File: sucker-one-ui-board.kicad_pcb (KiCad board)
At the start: 2 copper layers, 36.4 x 48.3 mm, 32 parts, among them J1 52271-1079, Q1 BSS138, SW1 LIFT, SW2 LOW, SW3 REVERSE, SW4 TRIGGER, SW5 DROP, SW6 HIGH, U1 WS2812-2020, U10 WS2812-2020, U11 WS2812-2020, U12 WS2812-2020, U2 WS2812-2020, U3 WS2812-2020, U4 WS2812-2020, U5 WS2812-2020, U6 WS2812-2020, U7 WS2812-2020, U8 WS2812-2020, U9 WS2812-2020

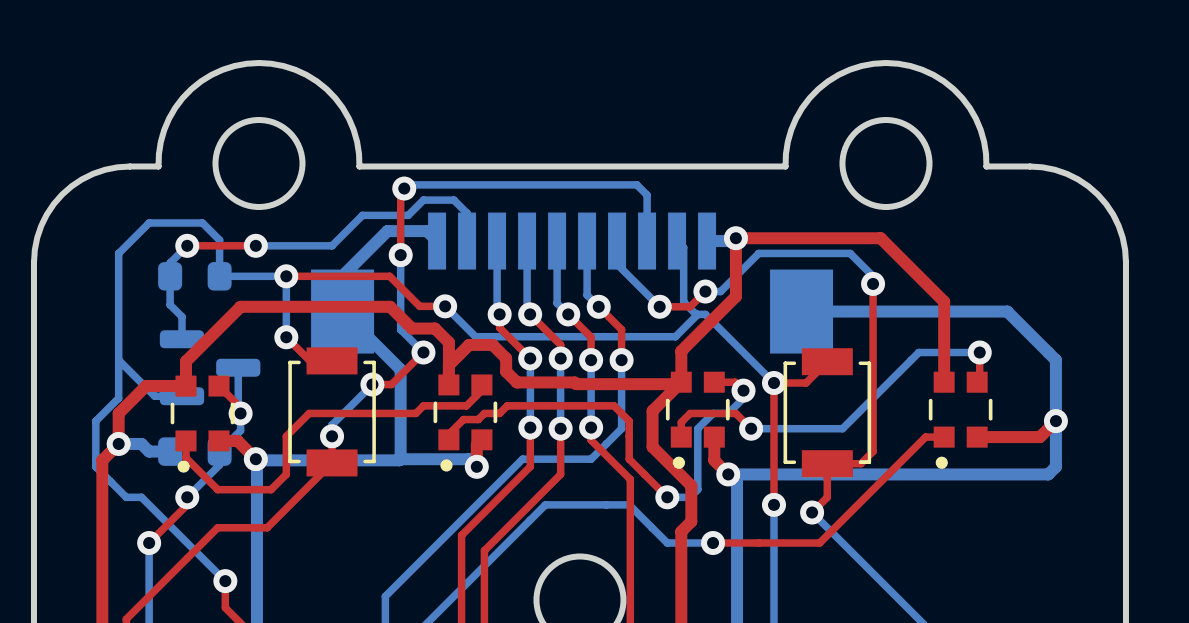
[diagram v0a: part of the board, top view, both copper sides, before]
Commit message: Flipped FFC connector and generated gerbers
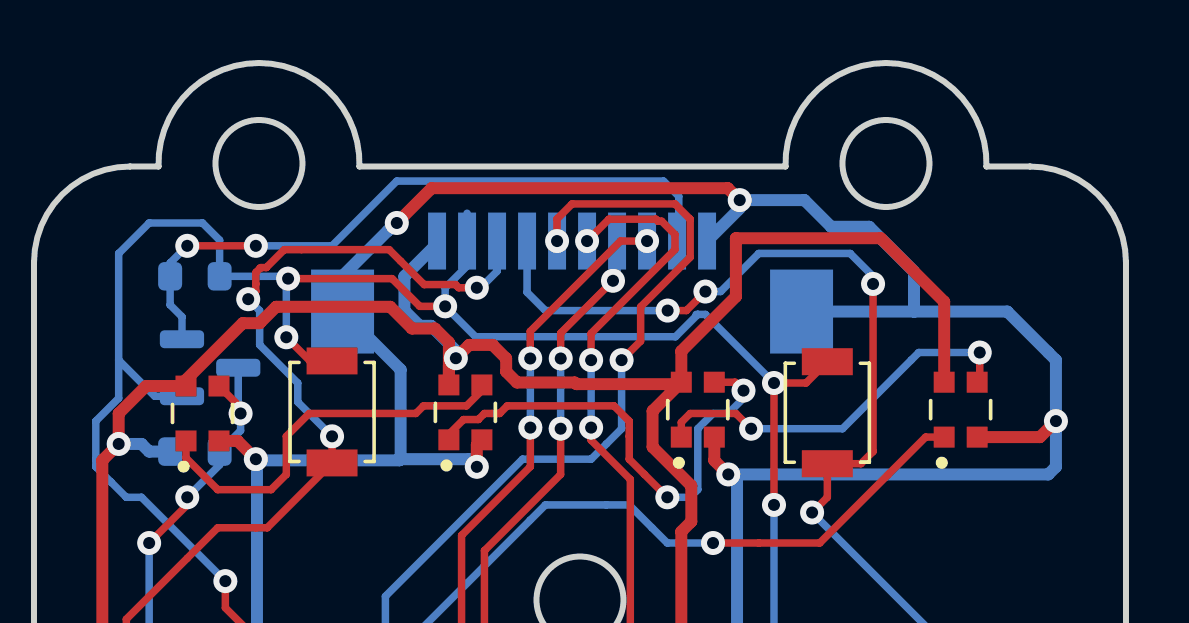
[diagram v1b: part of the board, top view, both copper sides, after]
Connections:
- J1 pad 1: +5V -> GND
- J1 pad 10: GND -> +5V
- J1 pad 2: +3V3 -> DATA_IN
- J1 pad 3: LIFT_BTN -> TRIGGER_BTN
- J1 pad 4: DROP_BTN -> REVERSE_BTN
- J1 pad 5: LOW_BTN -> HIGH_BTN
- J1 pad 6: HIGH_BTN -> LOW_BTN
- J1 pad 7: REVERSE_BTN -> DROP_BTN
- J1 pad 8: TRIGGER_BTN -> LIFT_BTN
- J1 pad 9: Net-(J1-Pad9) -> +3V3
- Q1 pad 2: Net-(J1-Pad9) -> DATA_IN
- R1 pad 1: Net-(J1-Pad9) -> DATA_IN
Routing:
- net DATA_IN: track 0.00 -> 22.5 mm, vias 0 -> 2
- net GND: track 162.8 -> 183.5 mm, vias 15 -> 17
- net Net-(J1-Pad9): track 15.4 -> 0.00 mm, vias 2 -> 0
- net LOW_BTN: track 68.9 -> 75.7 mm
- net HIGH_BTN: track 45.1 -> 49.5 mm
- net +5V: track 158.4 -> 162.3 mm
- net DROP_BTN: track 68.6 -> 72.3 mm
- net LIFT_BTN: track 65.3 -> 62.2 mm, vias 8 -> 6
- net TRIGGER_BTN: track 44.9 -> 46.6 mm
- net +3V3: track 105.1 -> 106.6 mm
- net REVERSE_BTN: track 65.1 -> 66.2 mm
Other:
- board text added: "5V"

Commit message: Updated and ordered ref 2
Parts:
- added C1: 100n, Capacitor_SMD:C_0603_1608Metric, F.Cu at (90.2, 89.9)
- added C2: 100n, Capacitor_SMD:C_0603_1608Metric, F.Cu at (73.6, 77.4)
- added C3: 100n, Capacitor_SMD:C_0603_1608Metric, F.Cu at (90.2, 77.4)
- added C4: 100n, Capacitor_SMD:C_0603_1608Metric, F.Cu at (73.6, 90.0)
- added C5: 100n, Capacitor_SMD:C_0603_1608Metric, F.Cu at (90.2, 102.4)
- added C6: 100n, Capacitor_SMD:C_0603_1608Metric, F.Cu at (73.6, 102.4)
- added C7: 50p, Capacitor_SMD:C_0603_1608Metric, B.Cu at (91.7, 69.6)
- moved TP8 39.0 mm to (66.4, 78.1)
- moved TP4 27.8 mm to (94.8, 77.7)
- moved TP2 27.6 mm to (69.2, 78.1)
- moved TP3 23.7 mm to (68.7, 90.3)
- moved TP5 22.5 mm to (68.7, 103.7)
- moved TP6 15.1 mm to (94.8, 90.8)
- moved TP10 9.31 mm to (69.5, 93.6)
- moved TP9 9.31 mm to (72.1, 93.6)
- moved TP1 9.31 mm to (74.6, 93.6)
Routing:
- net GND: track 183.5 -> 50.2 mm, vias 17 -> 28
- net +5V: track 162.3 -> 31.4 mm, vias 3 -> 21
- net LED_DATA: track 63.0 -> 10.7 mm, vias 3 -> 1
- net DROP_BTN: track 72.3 -> 24.3 mm, vias 6 -> 4
- net LIFT_BTN: track 62.2 -> 16.5 mm, vias 6 -> 2
- net LOW_BTN: track 75.7 -> 33.8 mm, vias 10 -> 6
- net HIGH_BTN: track 49.5 -> 30.6 mm, vias 6 -> 5
- net +3V3: track 106.6 -> 123.1 mm, vias 14 -> 3
- net DATA_IN: track 22.5 -> 34.4 mm, vias 2 -> 0
- net REVERSE_BTN: track 66.2 -> 58.0 mm
- net DO_LIFT: track 16.3 -> 11.9 mm, vias 2 -> 0
- net TRIGGER_BTN: track 46.6 -> 42.8 mm, vias 6 -> 5
- net Net-(U3-Pad1): track 14.5 -> 11.1 mm, vias 2 -> 0
- net Net-(U12-Pad3): track 10.9 -> 14.2 mm, vias 2 -> 0
- net Net-(U11-Pad3): track 11.2 -> 13.8 mm, vias 2 -> 0
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- added copper zone on In2.Cu, net +5V
- added copper zone on In1.Cu, net GND
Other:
- copper layers 2 -> 4
- board text added: "LED Orientation"
- board text removed: "Sucker One UI Board v1.0"

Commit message: Refactorings
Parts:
- removed Q1: BSS138, Package_TO_SOT_SMD:SOT-23
- removed R1, R2: 10k, Resistor_SMD:R_0603_1608Metric
- added kibuzzard-61084595: G***, kibuzzard-61084595, B.Cu at (69.5, 72.0)
- added kibuzzard-610845E2: G***, kibuzzard-610845E2, B.Cu at (69.2, 80.2)
- added kibuzzard-610845ED: G***, kibuzzard-610845ED, B.Cu at (94.8, 80.0)
- added kibuzzard-6108460F: G***, kibuzzard-6108460F, B.Cu at (68.8, 88.0)
- added kibuzzard-61084618: G***, kibuzzard-61084618, B.Cu at (94.8, 93.0)
- added kibuzzard-6108463B: G***, kibuzzard-6108463B, B.Cu at (93.7, 100.9)
- added kibuzzard-61084660: G***, kibuzzard-61084660, B.Cu at (68.7, 101.4)
- added kibuzzard-61084691: G***, kibuzzard-61084691, B.Cu at (69.5, 97.0)
- added kibuzzard-610846A8: G***, kibuzzard-610846A8, B.Cu at (72.1, 96.6)
- added kibuzzard-610846B1: G***, kibuzzard-610846B1, B.Cu at (74.7, 97.1)
- added kibuzzard-61084704: G***, kibuzzard-61084704, B.Cu at (82.8, 84.5)
- added kibuzzard-6108471A: G***, kibuzzard-6108471A, B.Cu at (82.6, 87.4)
- added kibuzzard-61084764: G***, kibuzzard-61084764, B.Cu at (82.0, 98.5)
- C7: moved to F.Cu
- J1: value 52271-1079 -> BM10B-SRSS-TB(LF)(SN); footprint Molex-52271-1079-*:Molex-52271-1079-Manufacturer_Recommended -> BM10B-SRSS-TB(LF)(SN):BM10B-SRSS-TB(LF)(SN)
- moved C7 18.1 mm to (73.7, 70.8), turned to 0 degrees
- moved TP8 8.80 mm to (69.6, 70.0)
- moved J1 4.13 mm to (82.0, 73.7)
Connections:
- C7 pad 1: DATA_IN -> LED_DATA
- J1 pad 2: DATA_IN -> LED_DATA
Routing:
- net DATA_IN: track 34.4 -> 0.00 mm
- net +3V3: track 123.1 -> 107.6 mm, vias 3 -> 2
- net LED_DATA: track 10.7 -> 25.1 mm, vias 1 -> 2
- net LIFT_BTN: track 16.5 -> 23.7 mm
- net LOW_BTN: track 33.8 -> 28.2 mm, vias 6 -> 4
- net TRIGGER_BTN: track 42.8 -> 37.2 mm, vias 5 -> 3
- net HIGH_BTN: track 30.6 -> 25.1 mm, vias 5 -> 3
- net REVERSE_BTN: track 58.0 -> 54.4 mm, vias 6 -> 4
- net DROP_BTN: track 24.3 -> 20.7 mm, vias 4 -> 2
- net +5V: track 31.4 -> 32.4 mm, vias 21 -> 19
- net GND: track 50.2 -> 51.1 mm, vias 28 -> 27
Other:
- board text added: "by Robin Reiter Hergatz, DE Aug 2021"
- board text removed: "+5V"
- board text removed: "DROP"
- board text removed: "HIGH"
- board text removed: "LED DATA"
- board text removed: "LIFT"
- board text removed: "LOW"
- board text removed: "REVERSE"
- board text removed: "TRIGGER"
